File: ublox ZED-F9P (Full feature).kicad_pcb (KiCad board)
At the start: 4 copper layers, 90 x 50 mm, 92 parts, among them J2 CONN_06NO_SILK_FEMALE_PTH, J4 Molex_PicoBlade, J6 CONN_06NO_SILK_FEMALE_PTH, J7 JST_GH, P1 USB_C_Plug_USB2.0, P2 USB_C_Plug_USB2.0, U1 LD1117S33TR, U3 ZED-F9P, U4 ZED-F9H

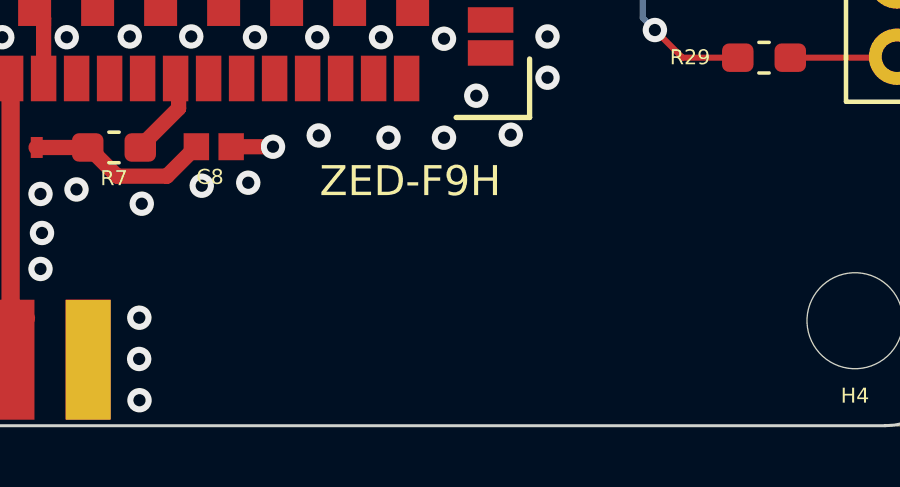
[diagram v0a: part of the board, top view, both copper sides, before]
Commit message: Add HGR logo
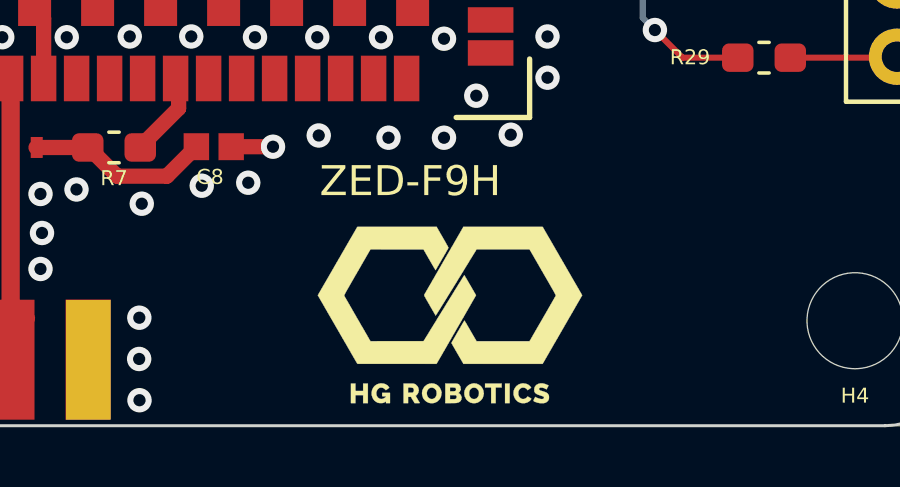
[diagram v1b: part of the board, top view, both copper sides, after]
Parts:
- added G***: LOGO, HG_Footprints:LOGO_HGR_1cm, B.Cu at (193.0, 96.2)

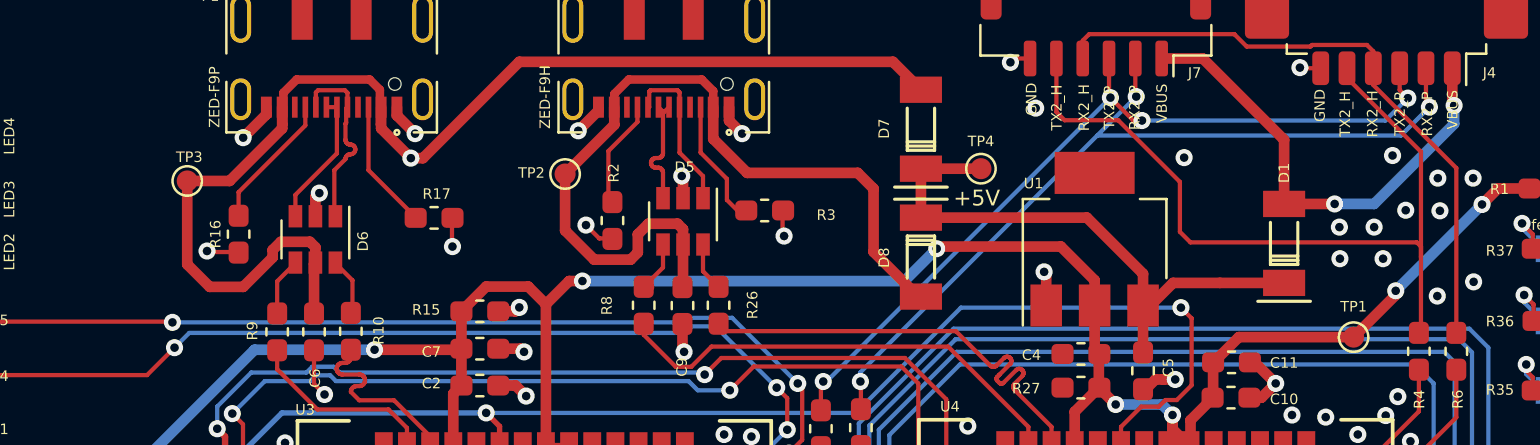
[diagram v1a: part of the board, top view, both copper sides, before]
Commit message: added silkscreen to testpoint
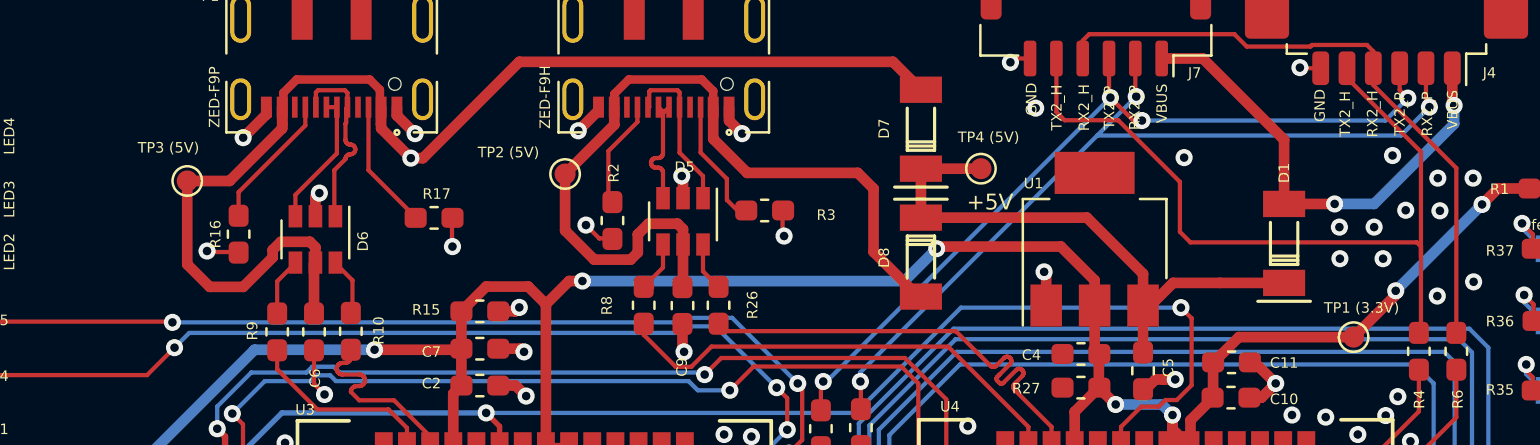
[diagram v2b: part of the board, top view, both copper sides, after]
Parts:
- TP1 (3.3V): renamed from TP1
- TP2 (5V): renamed from TP2
- TP3 (5V): renamed from TP3
- TP4 (5V): renamed from TP4
